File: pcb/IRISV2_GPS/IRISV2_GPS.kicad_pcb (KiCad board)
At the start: 4 copper layers, 50 x 50 mm, 15 parts, among them U1 NEO-M9N, U2 lna

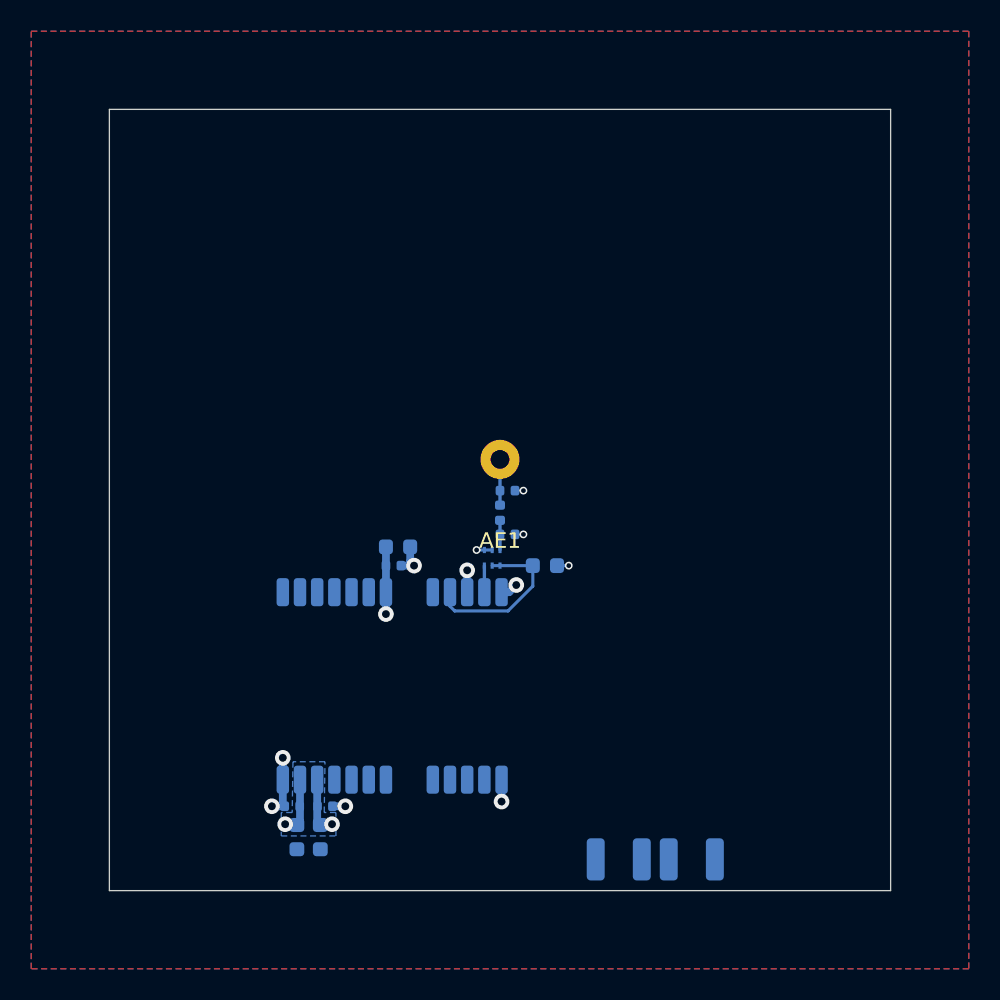
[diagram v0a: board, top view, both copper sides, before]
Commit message: gps finished minus tvs (WHY ARE THEY ALL 0201), top layout + routing started
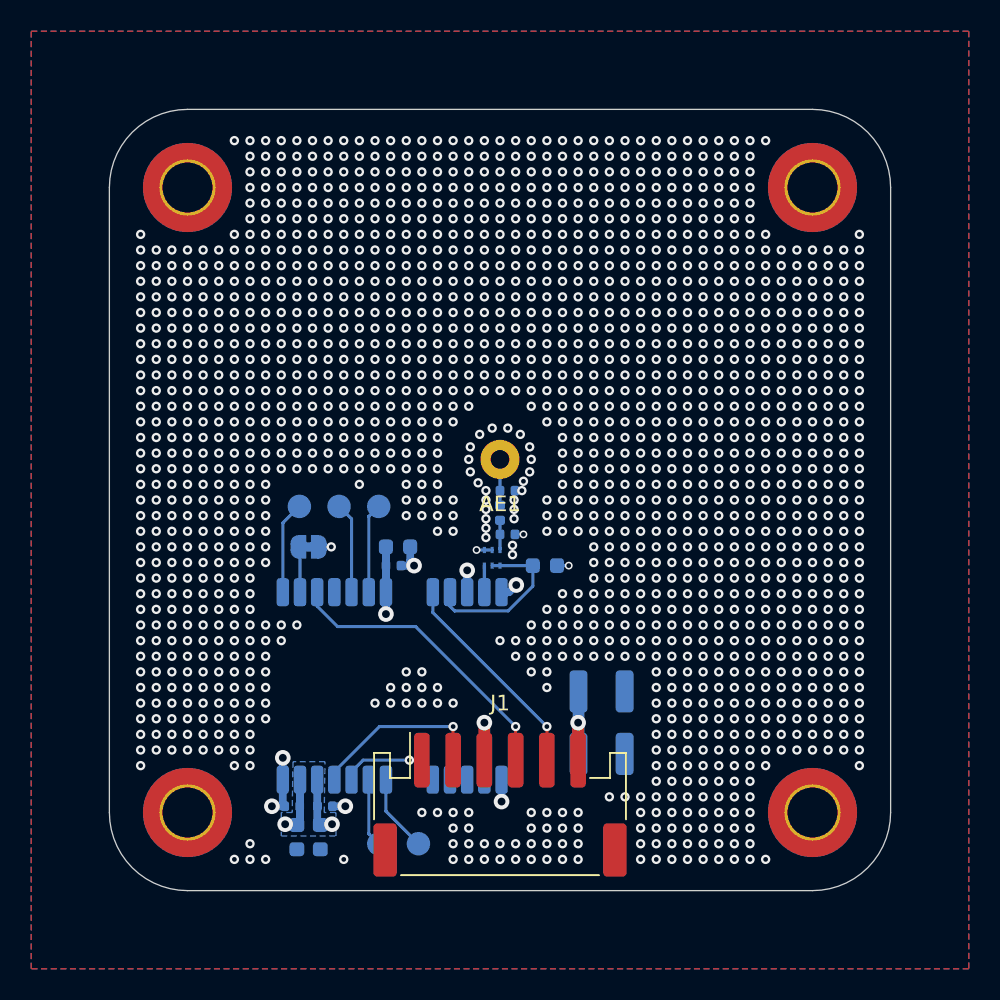
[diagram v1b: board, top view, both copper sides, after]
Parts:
- added BOOT: GPS_BOOT, TestPoint:TestPoint_Pad_D1.5mm, B.Cu at (137.2, 105.4)
- added D+: GPS_D+, TestPoint:TestPoint_Pad_D1.5mm, B.Cu at (142.2, 105.4)
- added D-: GPS_D-, TestPoint:TestPoint_Pad_D1.5mm, B.Cu at (139.7, 105.4)
- added DSEL: NC, Jumper:SolderJumper-2_P1.3mm_Bridged_RoundedPad1.0x1.5mm, B.Cu at (137.8, 108.0)
- added H1: MountingHole_Pad, MountingHole:MountingHole_3.2mm_M3_ISO7380_Pad_TopBottom, F.Cu at (170.0, 85.0)
- added H2: MountingHole_Pad, MountingHole:MountingHole_3.2mm_M3_ISO7380_Pad_TopBottom, F.Cu at (130.0, 85.0)
- added H3: MountingHole_Pad, MountingHole:MountingHole_3.2mm_M3_ISO7380_Pad_TopBottom, F.Cu at (130.0, 125.0)
- added H4: MountingHole_Pad, MountingHole:MountingHole_3.2mm_M3_ISO7380_Pad_TopBottom, F.Cu at (170.0, 125.0)
- added J1: Conn_01x06_MountingPin, Connector_JST:JST_PH_S6B-PH-SM4-TB_1x06-1MP_P2.00mm_Horizontal, F.Cu at (150.0, 124.5)
- added SCL: GPS_SCL, TestPoint:TestPoint_Pad_D1.5mm, B.Cu at (142.2, 127.0)
- added SDA: GPS_SDA, TestPoint:TestPoint_Pad_D1.5mm, B.Cu at (144.8, 127.0)
- moved C2 10.8 mm to (156.5, 117.2), turned to 0 degrees
- moved C1 8.88 mm to (156.5, 121.2)
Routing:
- net gps_pps: track 0.00 -> 18.9 mm, vias 0 -> 1
- net gps_rst: track 0.00 -> 13.8 mm, vias 0 -> 1
- net gps_mtx: track 0.00 -> 11.5 mm, vias 0 -> 1
- net Net-(U1-~{SAFEBOOT}): track 0.00 -> 5.93 mm
- net Net-(U1-USB_DM): track 0.00 -> 5.82 mm
- net Net-(U1-USB_DP): track 0.00 -> 5.76 mm
- net gps_mrx: track 0.00 -> 5.32 mm, vias 0 -> 1
- net Net-(U1-SDA/~{SPI_CS}): track 0.00 -> 4.96 mm
- net Net-(U1-SCL/SPI_CLK): track 0.00 -> 4.37 mm
- net +3.3V: track 29.4 -> 33.6 mm, vias 3 -> 5
- net Net-(JP1-B): track 0.00 -> 2.94 mm
- net GND: track 13.7 -> 15.6 mm, vias 11 -> 1567
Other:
- outline, holes or cut-outs redrawn

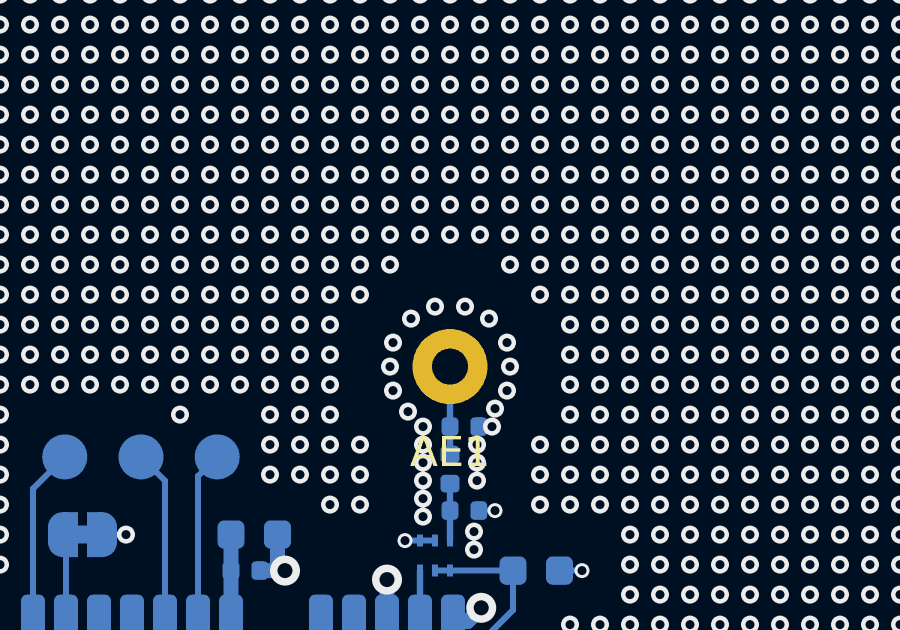
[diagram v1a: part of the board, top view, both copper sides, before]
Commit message: removed high g accel, top board layout looking decent, routing started also - though i realized i was missing the micro sd card and that's going to be a pain to add
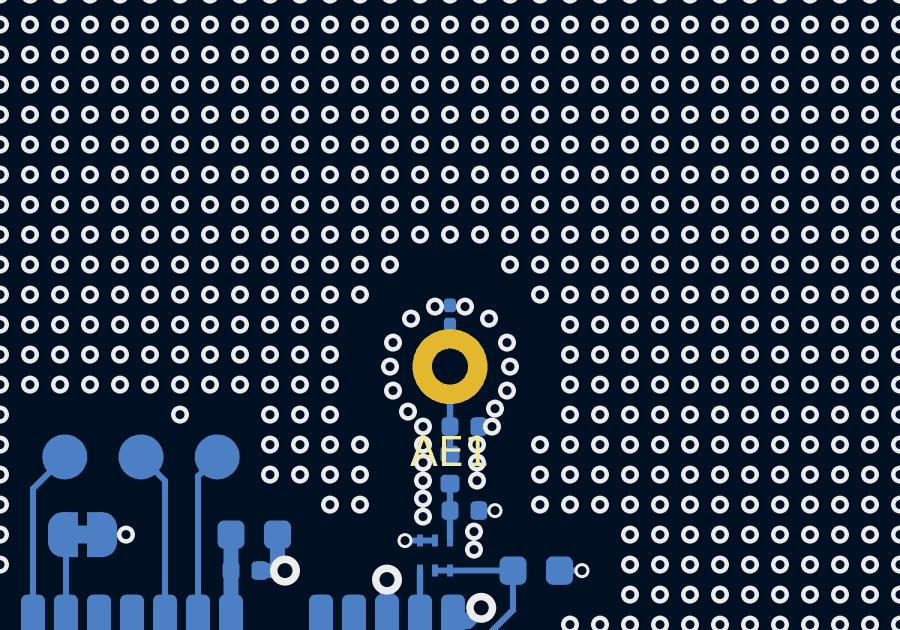
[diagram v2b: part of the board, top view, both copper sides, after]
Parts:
- added D1: D_TVS, Diode_SMD:D_0201_0603Metric, B.Cu at (150.0, 100.7)
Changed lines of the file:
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@@
+		)
+	)
+	(footprint "Diode_SMD:D_0201_0603Metric"
+		(layer "B.Cu")
+		(at 150 100.68 -90)
+		(descr "Diode SMD 0201 (0603 Metric), square (rectangular) end terminal, IPC-7351 nominal, (Body size source: https://www.vishay.com/docs/20052/crcw0201e3.pdf), generated with kicad-footprint-generator")
+		(tags "diode")
+		(property "Reference" "D1"
+			(at -1.52 0 180)
+			(layer "B.SilkS")
+			(effects
+				(font
+					(size 1 1)
+					(thickness 0.15)
+				)
+				(justify mirror)
+			)
+		)
+		(property "Value" "D_TVS"
+			(at 0 -1.05 90)
+			(layer "B.Fab")
+			(effects
+				(font
+					(size 1 1)
+					(thickness 0.15)
+				)
+				(justify mirror)
+			)
+		)
+		(property "Datasheet" "~"
+			(at 0 0 90)
+			(layer "B.Fab")
+			(hide yes)
+			(effects
+				(font
+					(size 1.27 1.27)
+					(thickness 0.15)
+				)
+				(justify mirror)
+			)
+		)
+		(property "Description" "Bidirectional transient-voltage-suppression diode"
+			(at 0 0 90)
+			(layer "B.Fab")
+			(hide yes)
+			(effects
+				(font
+					(size 1.27 1.27)
+					(thickness 0.15)
+				)
+				(justify mirror)
+			)
+		)
+		(property ki_fp_filters "TO-???* *_Diode_* *SingleDiode* D_*")
+		(sheetname "/")
+		(sheetfile "IRISV2_GPS.kicad_sch")
+		(attr smd)
+		(fp_circle
+			(center -0.86 0)
+			(end -0.81 0)
+			(stroke
+				(width 0.1)
+				(type solid)
+			)
+			(fill no)
+			(layer "B.SilkS")
+		)
+		(fp_rect
+			(start -0.7 0.35)
+			(end 0.7 -0.35)
+			(stroke
+				(width 0.05)
+				(type solid)
+			)
+			(fill no)
+			(layer "B.CrtYd")
+		)
+		(fp_line
+			(start -0.2 -0.15)
+			(end -0.2 0.15)
+			(stroke
+				(width 0.1)
+				(type solid)
+			)
+			(layer "B.Fab")
+		)
+		(fp_line
+			(start -0.1 -0.15)
+			(end -0.1 0.15)
+			(stroke
+				(width 0.1)
+				(type solid)
+			)
+			(layer "B.Fab")
+		)
+		(fp_rect
+			(start -0.3 0.15)
+			(end 0.3 -0.15)
+			(stroke
+				(width 0.1)
+				(type solid)
+			)
+			(fill no)
+			(layer "B.Fab")
+		)
+		(fp_text user "${REFERENCE}"
+			(at 0 0.68 90)
+			(layer "B.Fab")
+			(effects
+				(font
+					(size 0.25 0.25)
+					(thickness 0.04)
+				)
+				(justify mirror)
+			)
+		)
+		(pad "" smd roundrect
+			(at -0.345 0 270)
+			(size 0.318 0.36)
+			(layers "B.Paste")
+			(roundrect_rratio 0.25)
+		)
+		(pad "" smd roundrect
+			(at 0.345 0 270)
+			(size 0.318 0.36)
+			(layers "B.Paste")
+			(roundrect_rratio 0.25)
+		)
+		(pad "1" smd roundrect
+			(at -0.32 0 270)
+			(size 0.46 0.4)
+			(layers "B.Cu" "B.Mask")
+			(roundrect_rratio 0.25)
+			(net 2 "GND")
+			(pinfunction "A1")
+			(pintype "passive")
+		)
+		(pad "2" smd roundrect
+			(at 0.32 0 270)
+			(size 0.46 0.4)
+			(layers "B.Cu" "B.Mask")
+			(roundrect_rratio 0.25)
+			(net 1 "Net-(AE1-A)")
+			(pinfunction "A2")
+			(pintype "passive")
+		)
+		(embedded_fonts no)
+		(model "${KICAD9_3DMODEL_DIR}/Diode_SMD.3dshapes/D_0201_0603Metric.step"
+			(offset
+				(xyz 0 0 0)
+			)
+			(scale
+				(xyz 1 1 1)
+			)
+			(rotate
+				(xyz 0 0 0)
+			)
 		)
 	)
@@
 		(at 149.5 108.7 -90)
 		(property "Reference" "U2"
-			(at -0.2 2.25 0)
+			(at -0.5 2.1 0)
 			(unlocked yes)
 			(layer "B.SilkS")
@@
 		(tags "capacitor")
 		(property "Reference" "C10"
-			(at -2.02 -0.05 0)
+			(at -2.52 -0.6 0)
 			(layer "B.SilkS")
 			(effects
@@
 		(tags "capacitor")
 		(property "Reference" "C7"
-			(at 1.07 0.05 180)
-			(layer "B.SilkS")
-			(effects
+			(at 2.62 0.2 180)
+			(layer "B.SilkS")
+			(effects
